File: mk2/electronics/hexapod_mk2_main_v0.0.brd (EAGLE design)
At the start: 84.5 x 61 mm, 22 parts, among them U1 74LVC1T45GW,125TSSOP6_SOT363-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

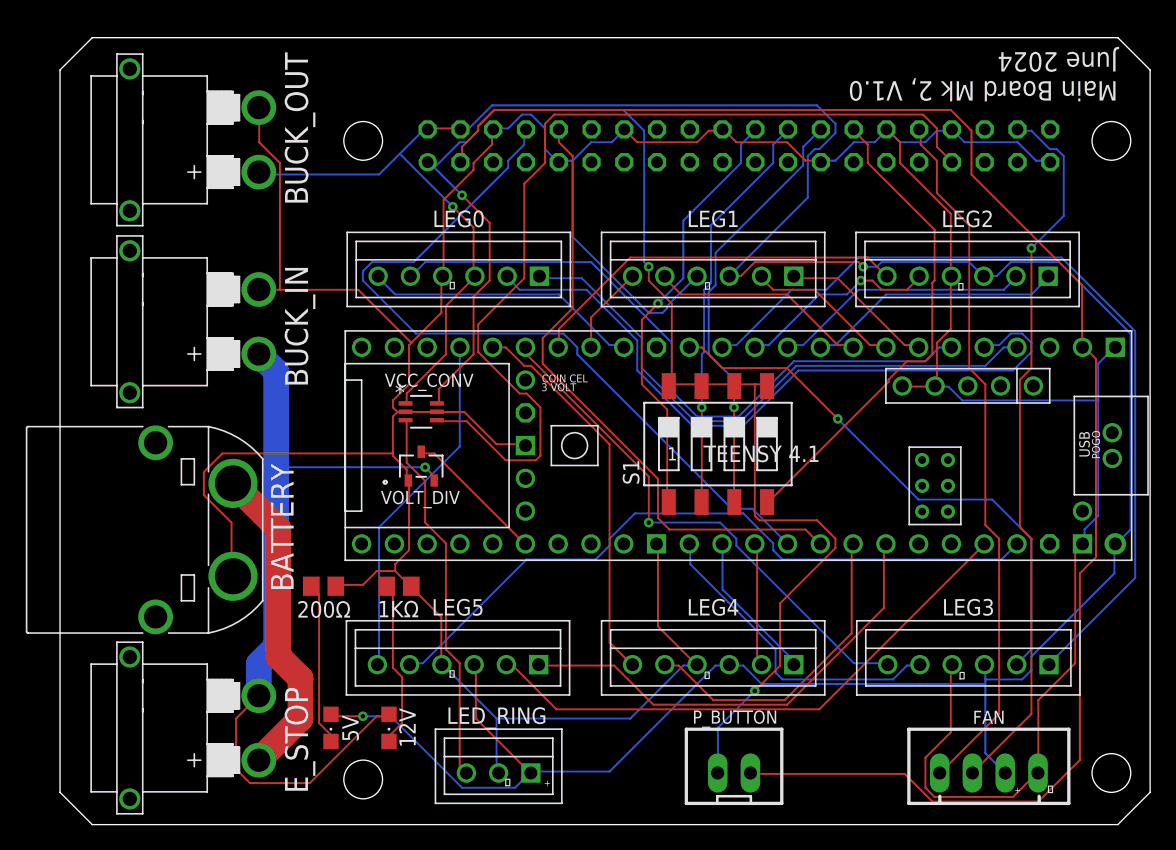
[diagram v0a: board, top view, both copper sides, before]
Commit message: fix autorouting issues
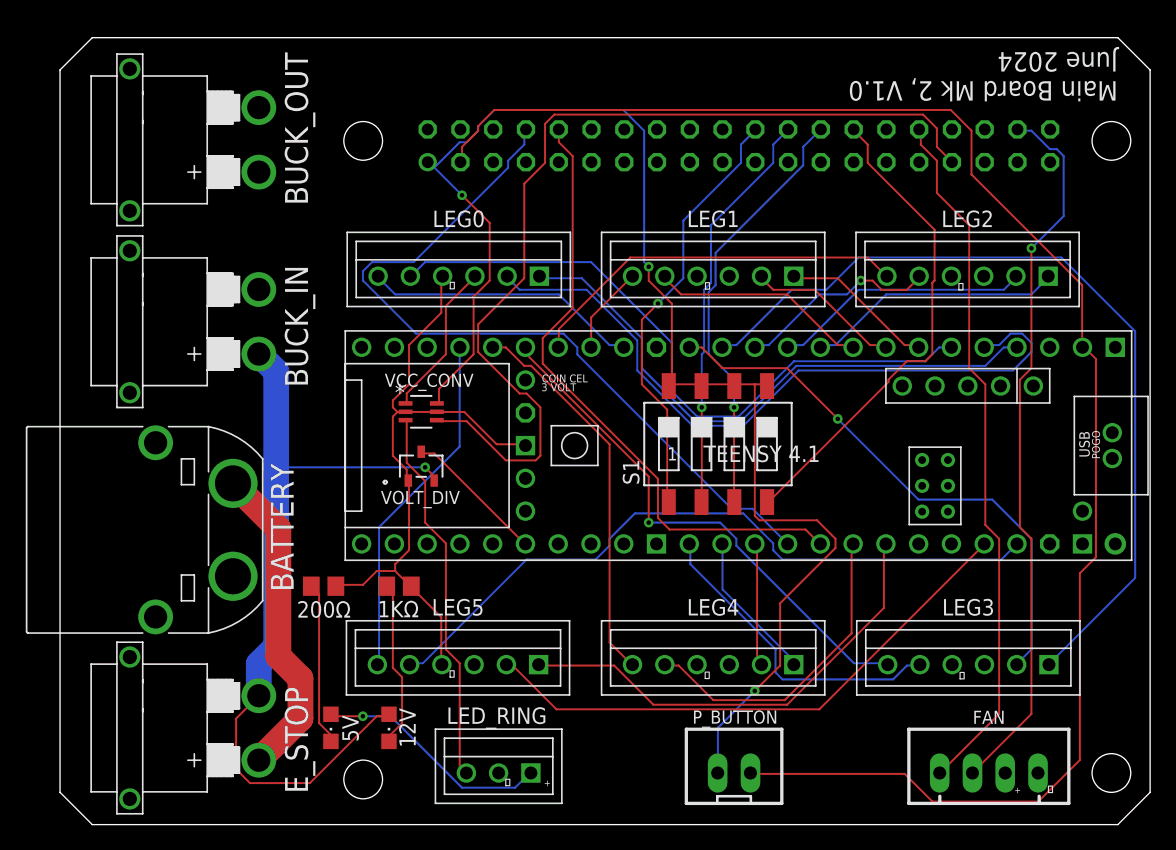
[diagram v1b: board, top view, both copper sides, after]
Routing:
- net GND: track 319.9 -> 50.6 mm
- net 5V: track 232.4 -> 30.4 mm, vias 3 -> 1
